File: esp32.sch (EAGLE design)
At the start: 70 parts, among them IC1 PEC11R-4230K-S00243D, IC2 AD8532ARZ, IC3 MCP1700T-3302E_TT, IC4 MCP1700T-3302E_TT, T1 BST82-1, T2 BST82-1, T3 BST82-1, U1 ESP32-WROOM-32D, X1 JST-XH-02-PIN-LONG-PAD, X2 JST-XH-03-PIN-LONG-PAD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

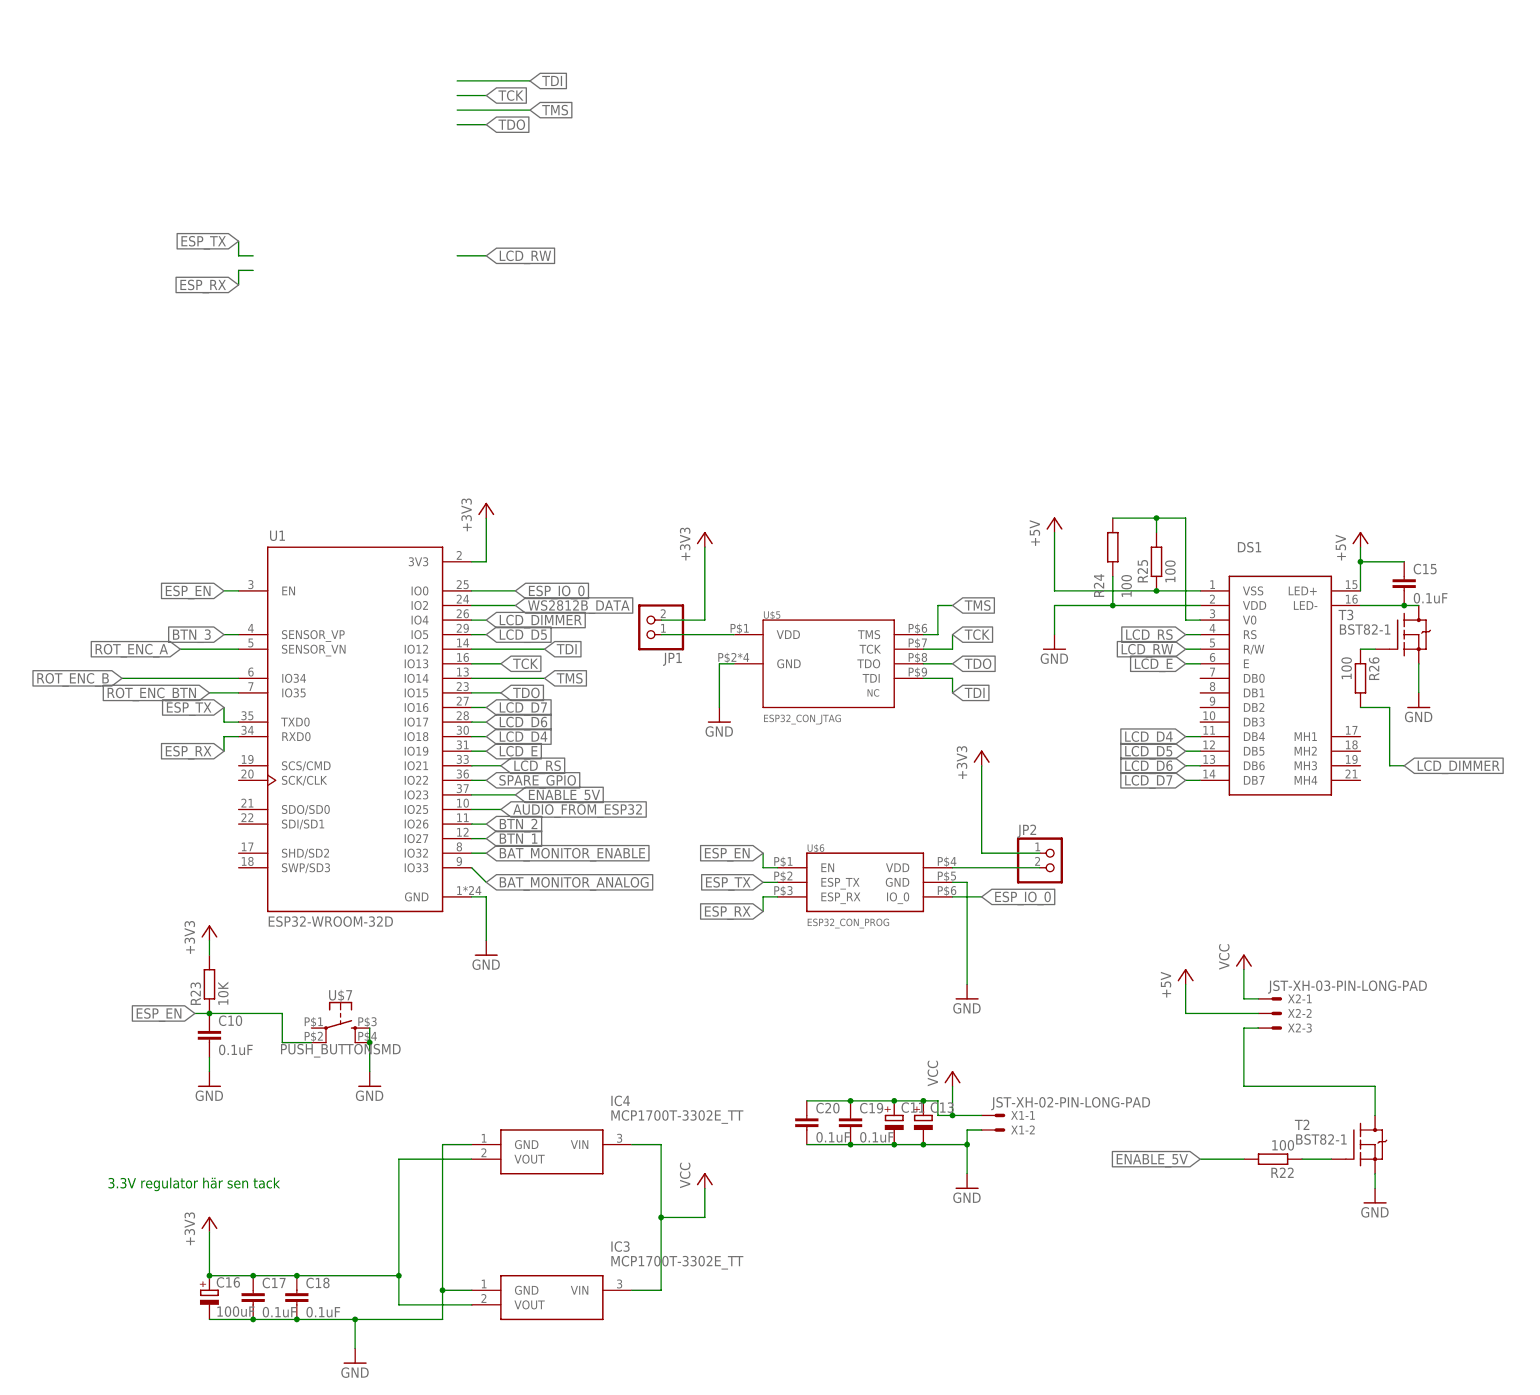
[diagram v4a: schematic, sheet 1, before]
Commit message: Tror fan att den är färdig nu, allt som ska bli SMT är SMT nu och rätt pinnar för rätt sak förhoppningsvis.
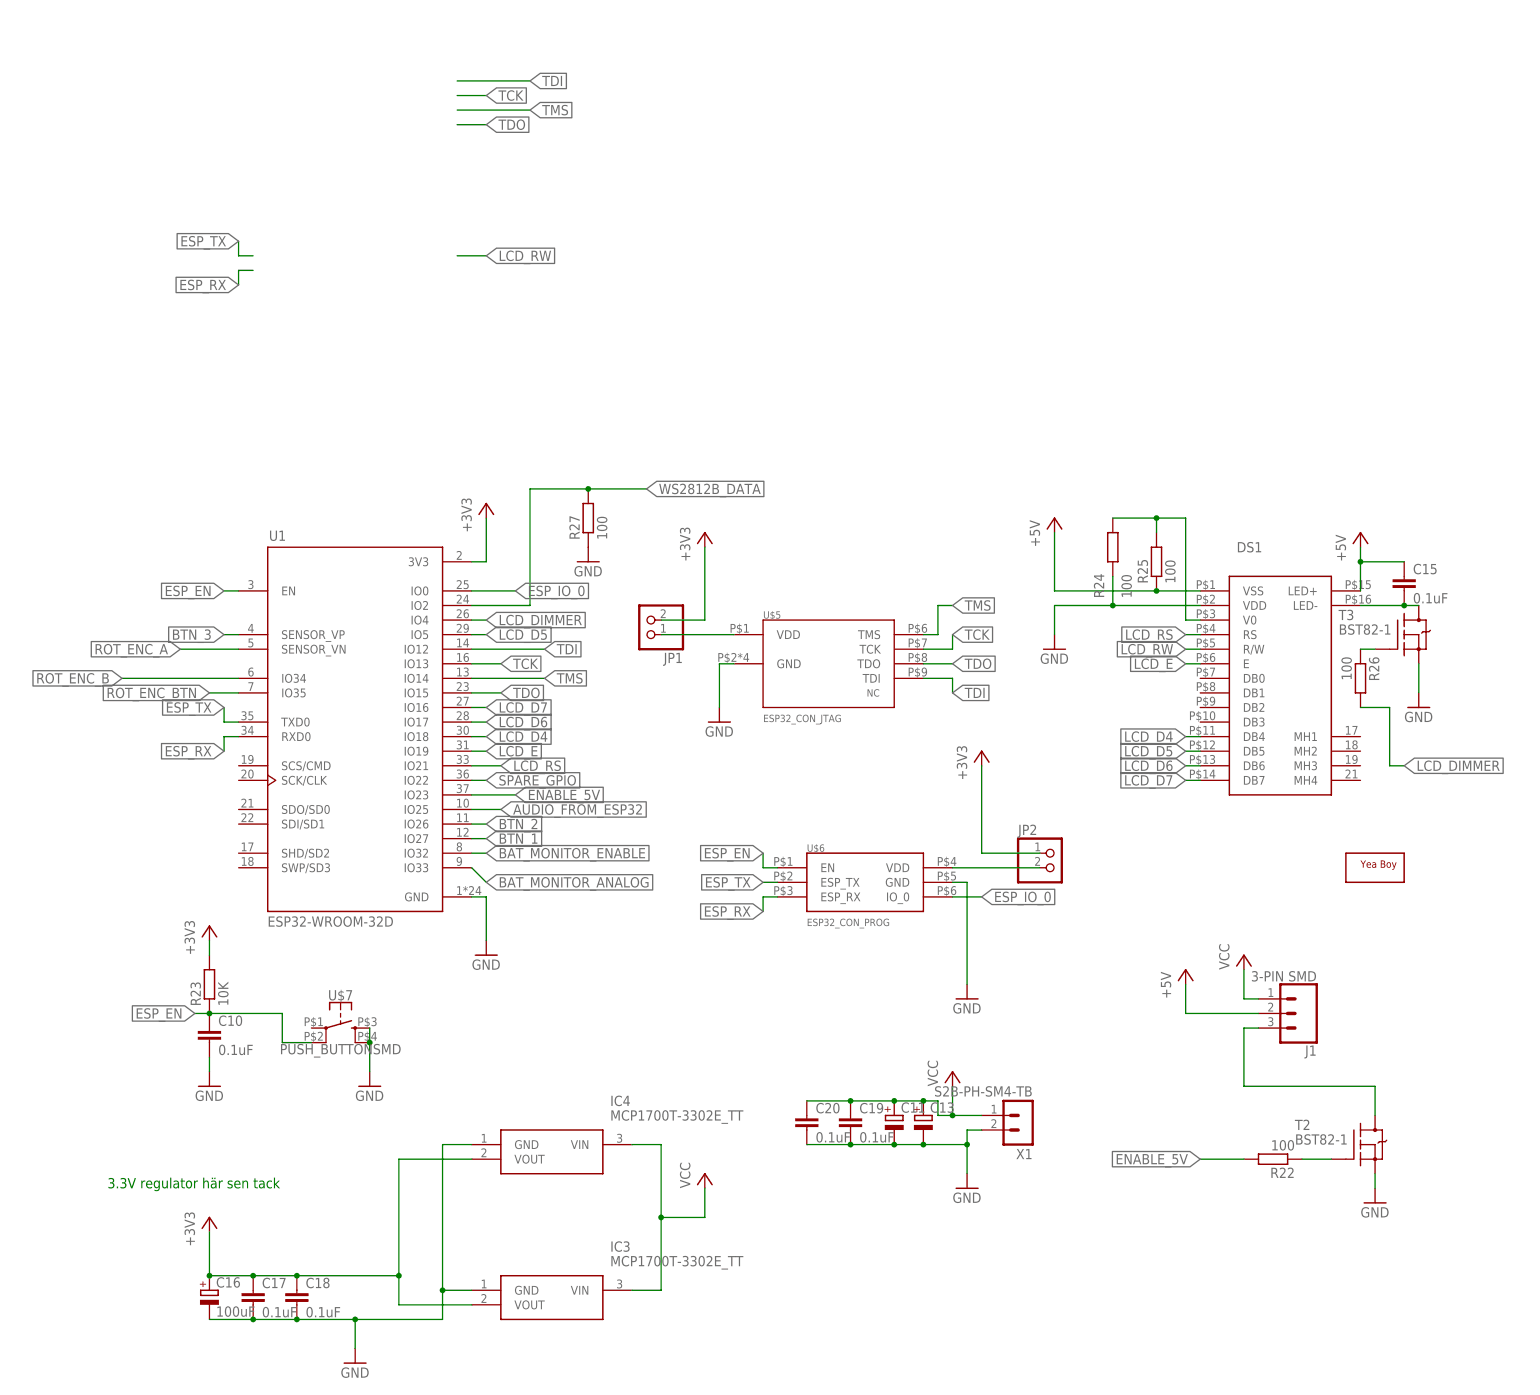
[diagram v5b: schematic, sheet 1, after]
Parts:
- removed X2, X3: JST-XH-03-PIN-LONG-PAD, Rembrandt Electronics - JST XH Connectors v1-0:JST-XH-03-PIN-LONG-PAD
- removed X4: JST-XH-02-PIN-LONG-PAD, Rembrandt Electronics - JST XH Connectors v1-0:JST-XH-02-PIN-LONG-PAD
- added J1, J2: 3-PIN SMD, SparkFun-Connectors:CONN_03JST-SMD
- added J3: (no value), SparkFun-Connectors:CONN_02-JST-2MM-SMT
- added R27: 100, rcl:R-EU_R0603
- added U$8: TOUCHMARK, Test:TOUCHMARK
- DS1: device Test:NHD-0216XZ-FSW-GBWNHD0216XZFSWGBW_DUPONTCONNECTOR -> Test:NHD-0216XZ-FSW-GBWSMT
- X1: value JST-XH-02-PIN-LONG-PAD -> S2B-PH-SM4-TB; device Rembrandt Electronics - JST XH Connectors v1-0:JST-XH-02-PIN-LONG-PAD -> con-JST PH:S2B-PH-SM4-TB
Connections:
- net +5V: now also J1.2, J2.3; no longer X2-2.S, X3-1.S
- net GND: now also J2.1, J3.2, R27.1, X1.2; no longer X1-2.S, X3-3.S, X4-2.S
- net N$15: now also J1.3; no longer X2-3.S
- net SPEAKER_OUT: now also J3.1; no longer X4-1.S
- net VCC: now also J1.1, X1.1; no longer X1-1.S, X2-1.S
- net WS2812B_DATA: now also J2.2, R27.2; no longer X3-2.S
